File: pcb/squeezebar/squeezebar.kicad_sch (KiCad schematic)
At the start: 41 parts

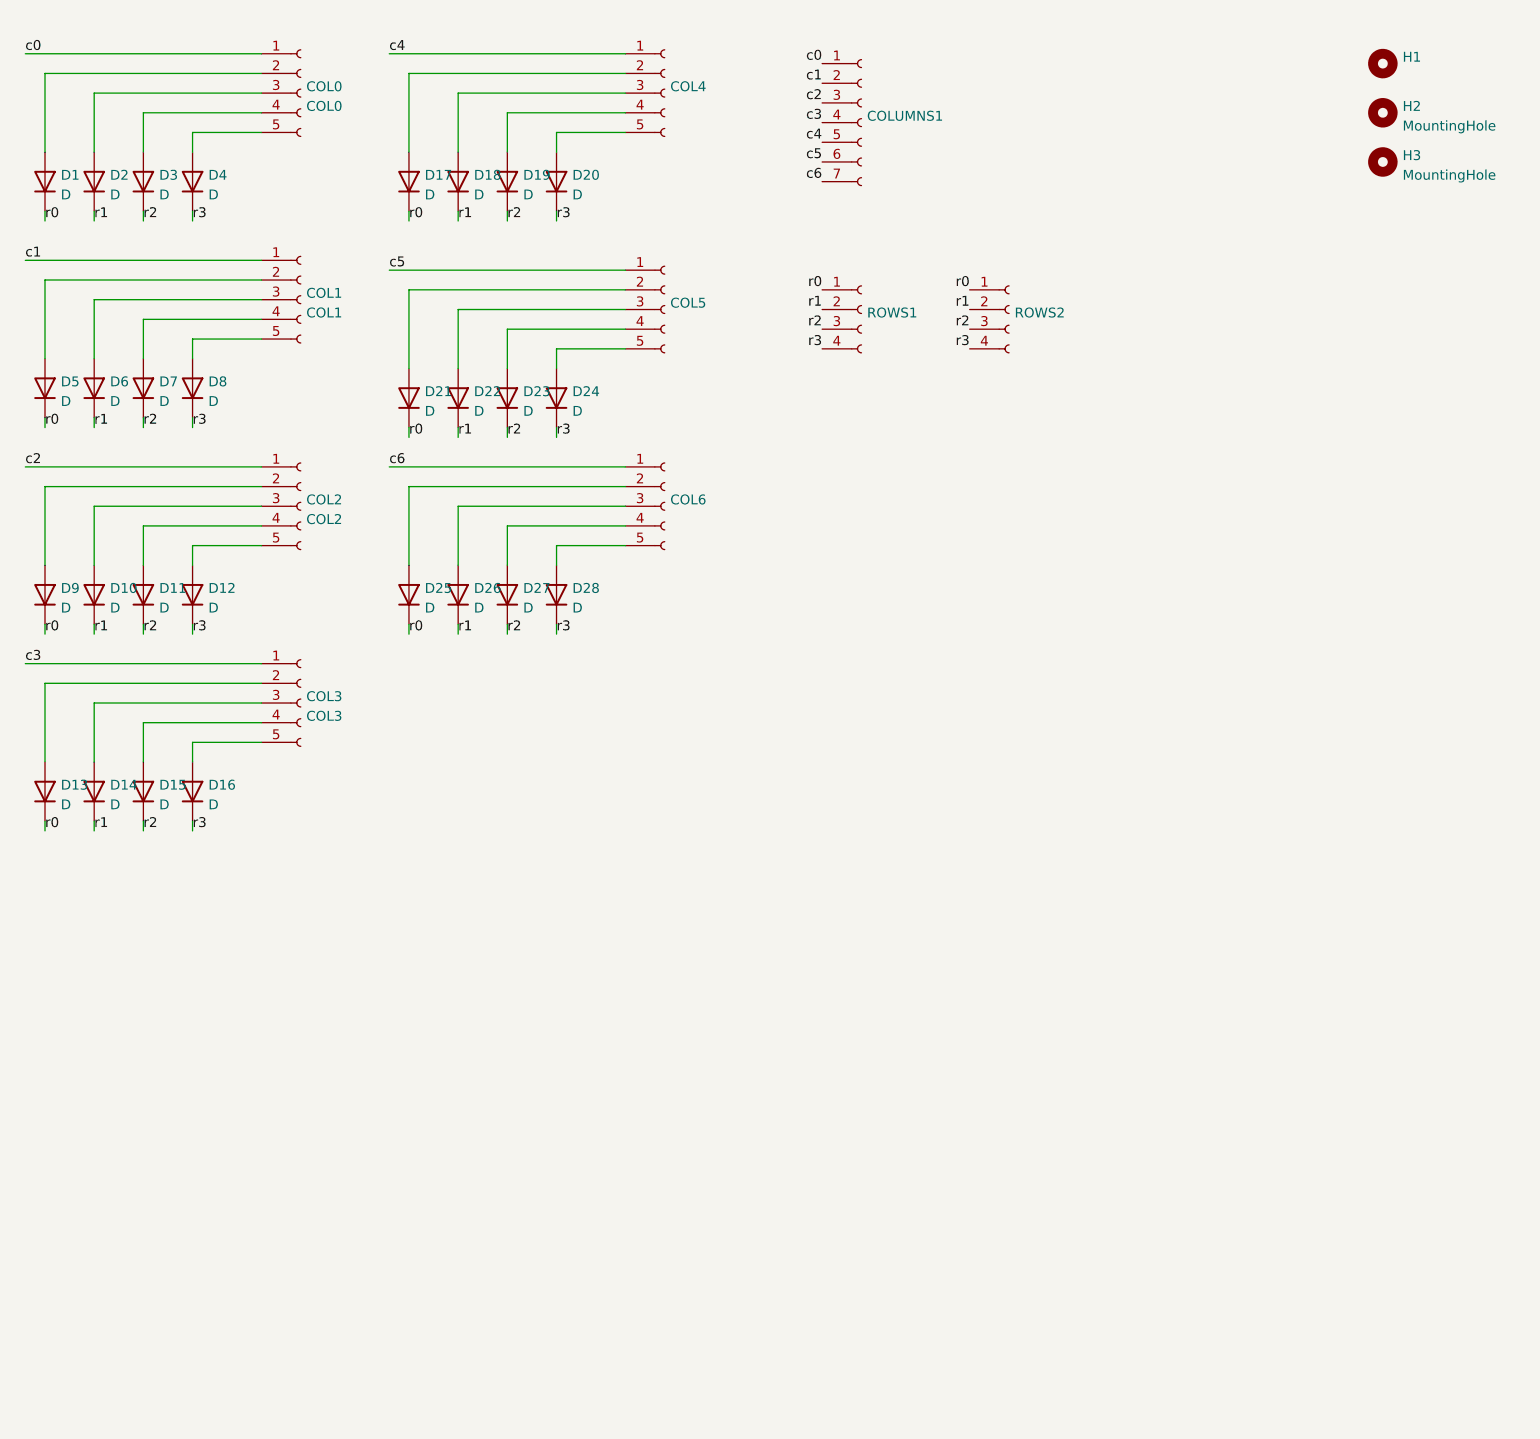
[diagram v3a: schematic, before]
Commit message: Squeezebar PCB: Add MCU. It's no longer a daughterboard...
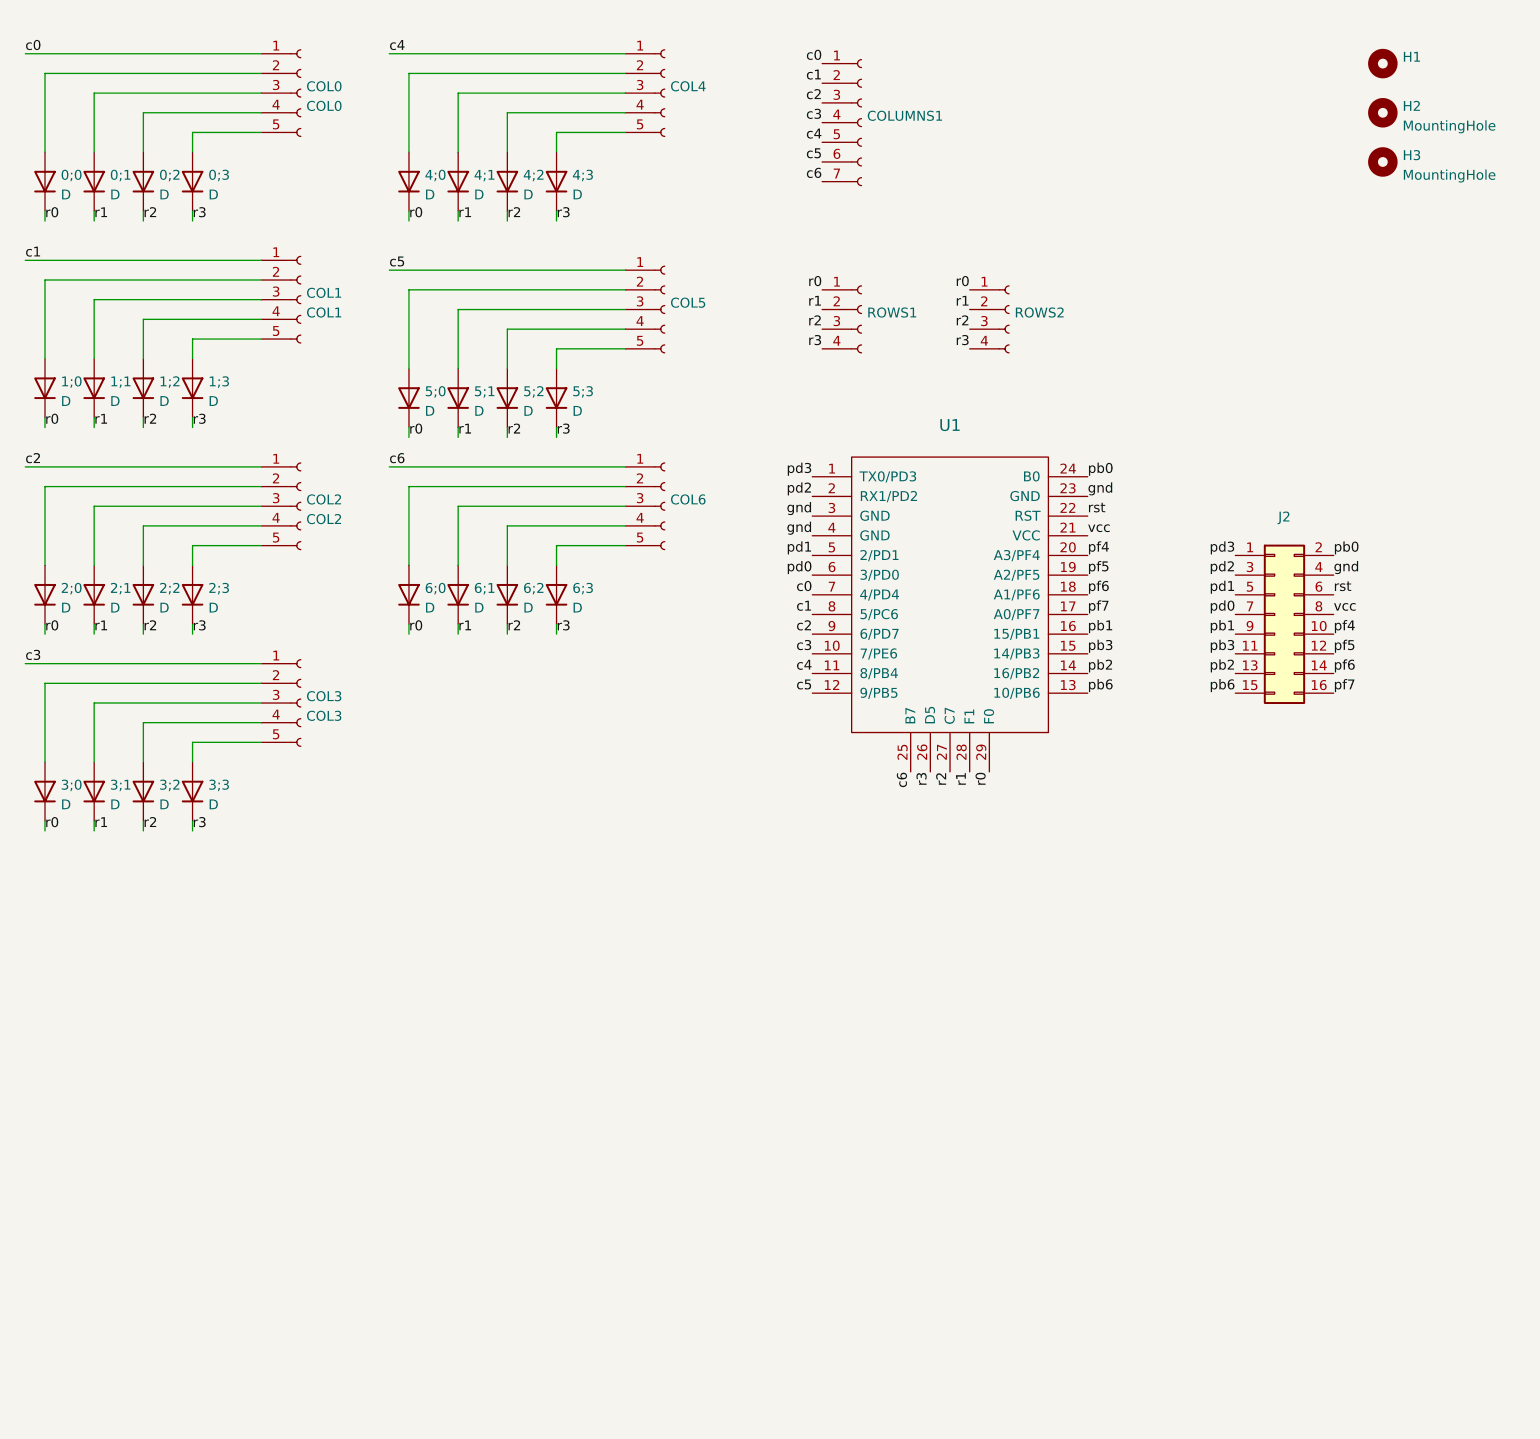
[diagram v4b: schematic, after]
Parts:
- added J2: (no value), symbol Connector_Generic:Conn_02x08_Odd_Even
- added U1: (no value), symbol keebio:Elite-C
- renumbered D1 to 0;0, D2 to 0;1, D3 to 0;2, D4 to 0;3, D5 to 1;0, D6 to 1;1, D7 to 1;2, D8 to 1;3, D9 to 2;0, D10 to 2;1, D11 to 2;2, D12 to 2;3, D13 to 3;0, D14 to 3;1, D15 to 3;2, D16 to 3;3, D17 to 4;0, D18 to 4;1, D19 to 4;2, D20 to 4;3, D21 to 5;0, D22 to 5;1, D23 to 5;2, D24 to 5;3, D25 to 6;0, D26 to 6;1, D27 to 6;2, D28 to 6;3
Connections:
- net c0: now also U1.7 (4/PD4)
- net c1: now also U1.8 (5/PC6)
- net c2: now also U1.9 (6/PD7)
- net c3: now also U1.10 (7/PE6)
- net c4: now also U1.11 (8/PB4)
- net c5: now also U1.12 (9/PB5)
- net c6: now also U1.25 (B7)
- net r0: now also U1.29 (F0)
- net r1: now also U1.28 (F1)
- net r2: now also U1.27 (C7)
- net r3: now also U1.26 (D5)
- new net gnd: J2.4 (Pin_4), U1.23 (GND), U1.3 (GND), U1.4 (GND)
- new net pb0: J2.2 (Pin_2), U1.24 (B0)
- new net pb1: J2.9 (Pin_9), U1.16 (15/PB1)
- new net pb2: J2.13 (Pin_13), U1.14 (16/PB2)
- new net pb3: J2.11 (Pin_11), U1.15 (14/PB3)
- new net pb6: J2.15 (Pin_15), U1.13 (10/PB6)
- new net pd0: J2.7 (Pin_7), U1.6 (3/PD0)
- new net pd1: J2.5 (Pin_5), U1.5 (2/PD1)
- new net pd2: J2.3 (Pin_3), U1.2 (RX1/PD2)
- new net pd3: J2.1 (Pin_1), U1.1 (TX0/PD3)
- new net pf4: J2.10 (Pin_10), U1.20 (A3/PF4)
- new net pf5: J2.12 (Pin_12), U1.19 (A2/PF5)
- new net pf6: J2.14 (Pin_14), U1.18 (A1/PF6)
- new net pf7: J2.16 (Pin_16), U1.17 (A0/PF7)
- new net rst: J2.6 (Pin_6), U1.22 (RST)
- new net vcc: J2.8 (Pin_8), U1.21 (VCC)

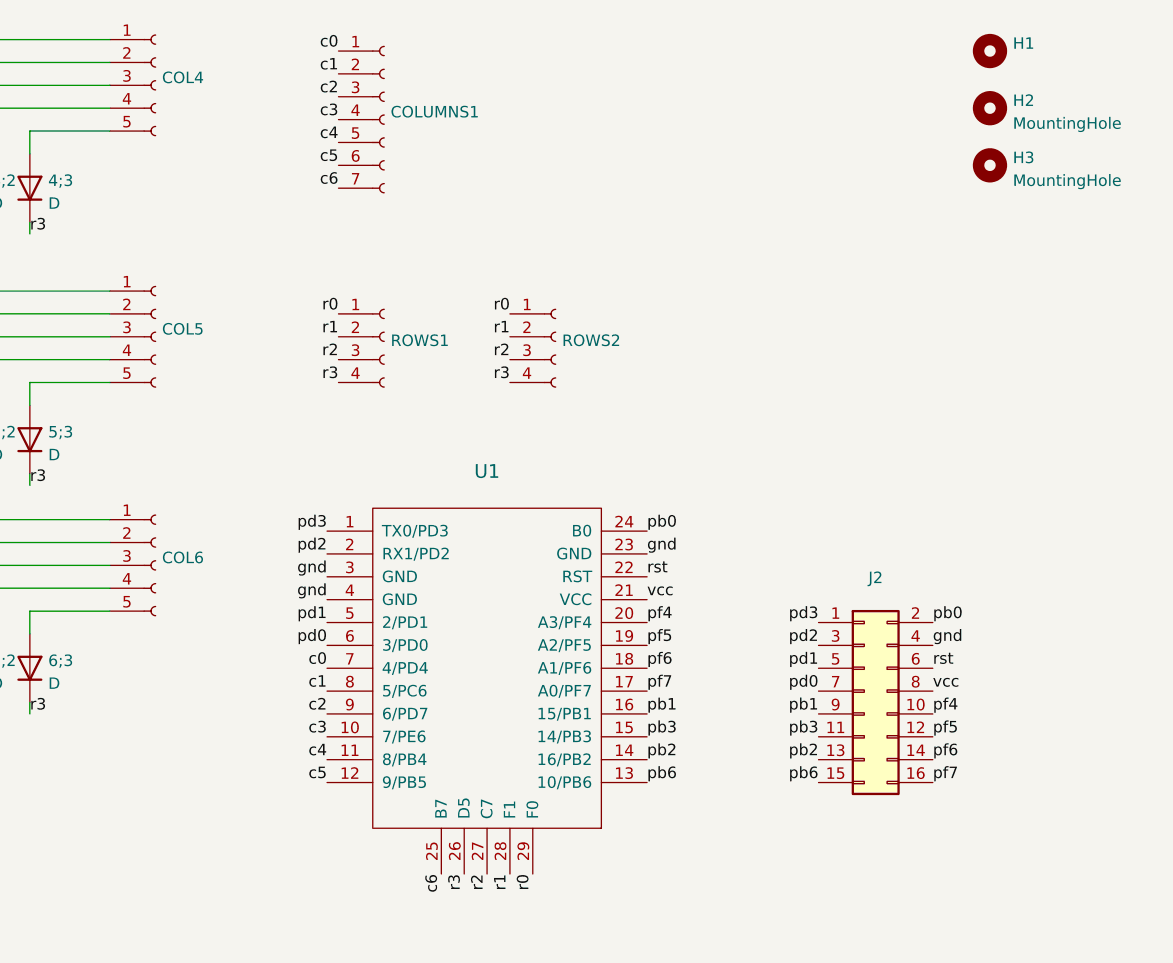
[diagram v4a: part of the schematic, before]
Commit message: MatrixBar: Use Pro Micro pins for the rows/cols
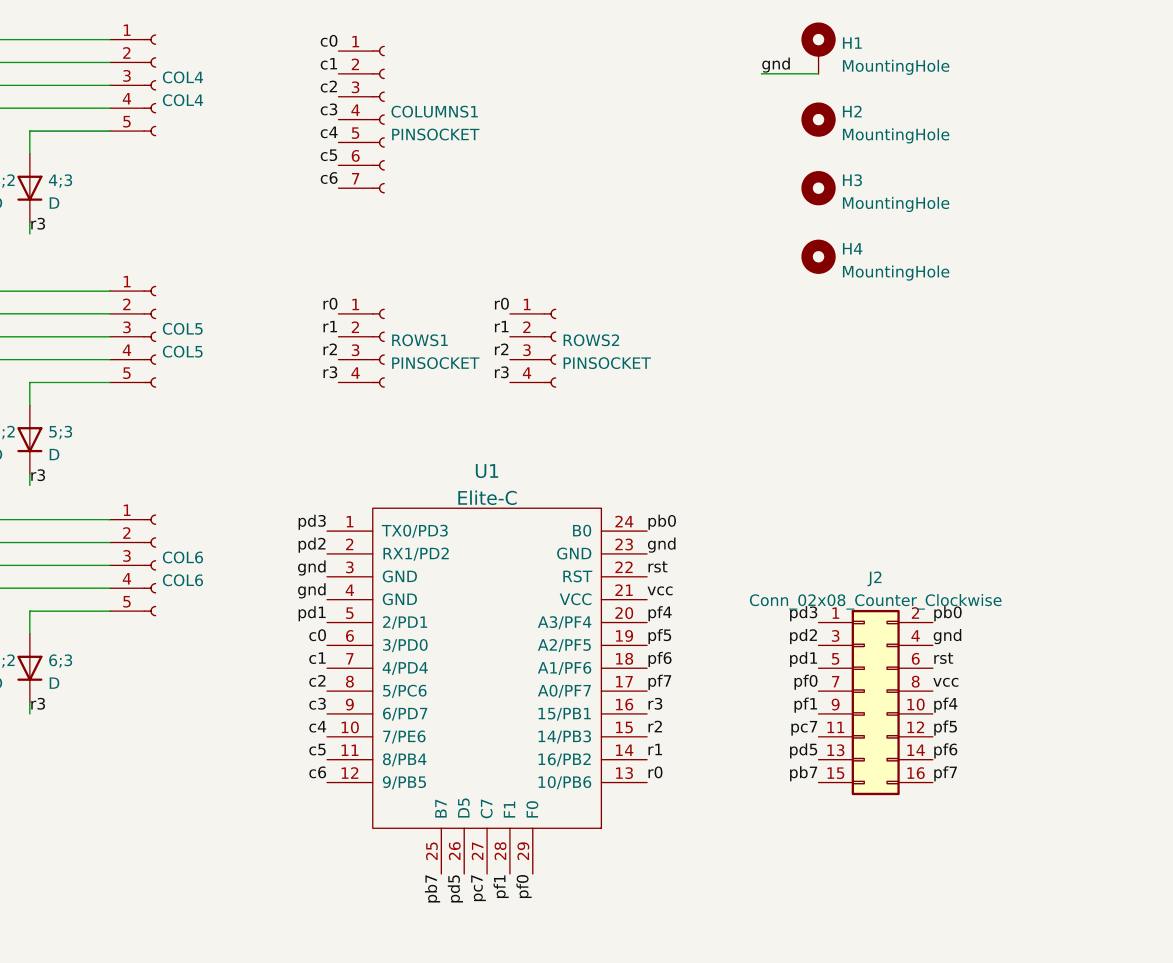
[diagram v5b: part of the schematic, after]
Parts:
- added H4: MountingHole, symbol Mechanical:MountingHole
- 0;0, 0;1, 0;2, 0;3, 1;0, 1;1, 1;2, 1;3, 2;0, 2;1, 2;2, 2;3, 3;0, 3;1, 3;2, 3;3, 4;0, 4;1, 4;2, 4;3, 5;0, 5;1, 5;2, 5;3, 6;0, 6;1, 6;2, 6;3: footprint (none) -> Library:Diode
- COL4: value (none) -> COL4
- COL5: value (none) -> COL5
- COL6: value (none) -> COL6
- COLUMNS1: value (none) -> PINSOCKET; footprint (none) -> Connector_PinHeader_2.54mm:PinHeader_1x07_P2.54mm_Vertical
- H1: value (none) -> MountingHole; footprint (none) -> MountingHole:MountingHole_2.2mm_M2_DIN965_Pad; symbol Mechanical:MountingHole -> Mechanical:MountingHole_Pad
- H3: footprint MountingHole:MountingHole_2.2mm_M2_DIN965 -> (none)
- J2: value (none) -> Conn_02x08_Counter_Clockwise; footprint (none) -> Library:PinSocket_2x08_P2.54mm_Bespoke
- ROWS1, ROWS2: value (none) -> PINSOCKET; footprint (none) -> Library:PinSocket_1x04_P2.54mm_Vertical_LongPads
- U1: value (none) -> Elite-C; footprint (none) -> 3dmodels:Elite-C
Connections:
- net c0: now also U1.6 (3/PD0); no longer U1.7 (4/PD4)
- net c1: now also U1.7 (4/PD4); no longer U1.8 (5/PC6)
- net c2: now also U1.8 (5/PC6); no longer U1.9 (6/PD7)
- net c3: now also U1.9 (6/PD7); no longer U1.10 (7/PE6)
- net c4: now also U1.10 (7/PE6); no longer U1.11 (8/PB4)
- net c5: now also U1.11 (8/PB4); no longer U1.12 (9/PB5)
- net c6: now also U1.12 (9/PB5); no longer U1.25 (B7)
- net gnd: now also H1.1
- net r0: now also U1.13 (10/PB6); no longer U1.29 (F0)
- net r1: now also U1.14 (16/PB2); no longer U1.28 (F1)
- net r2: now also U1.15 (14/PB3); no longer U1.27 (C7)
- net r3: now also U1.16 (15/PB1); no longer U1.26 (D5)
- net pb1 renamed pf1
- net pf1: now also U1.28 (F1); no longer U1.16 (15/PB1)
- net pb2 renamed pd5
- net pd5: now also U1.26 (D5); no longer U1.14 (16/PB2)
- net pb3 renamed pc7
- net pc7: now also U1.27 (C7); no longer U1.15 (14/PB3)
- net pb6 renamed pb7
- net pb7: now also U1.25 (B7); no longer U1.13 (10/PB6)
- net pd0 renamed pf0
- net pf0: now also U1.29 (F0); no longer U1.6 (3/PD0)
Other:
- moved on the sheet: H2, H3

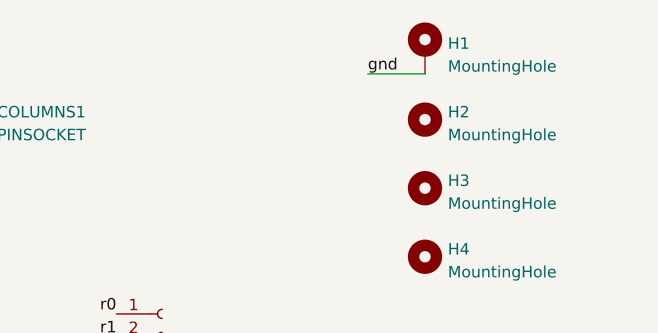
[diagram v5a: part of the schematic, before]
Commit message: Switch to M3 screws
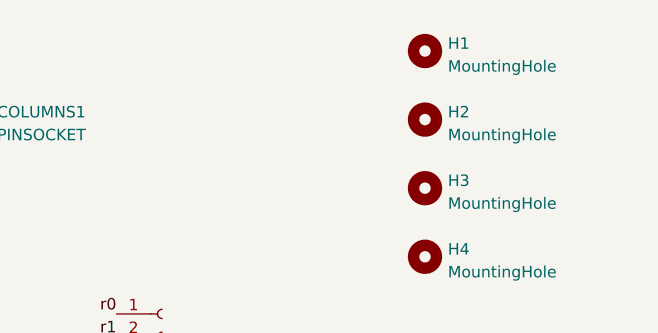
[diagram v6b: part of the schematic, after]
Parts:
- H1: footprint MountingHole:MountingHole_2.2mm_M2_DIN965_Pad -> (none); symbol Mechanical:MountingHole_Pad -> Mechanical:MountingHole
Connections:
- net gnd: no longer H1.1
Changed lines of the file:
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@@
-    (stroke (width 0) (type default) (color 0 0 0 0))
-  )
-  (wire (pts (xy 171.45 24.13) (xy 177.8 24.13))
     (stroke (width 0) (type default) (color 0 0 0 0))
   )
@@
   )
   (label "r3" (at 43.18 41.91 0)
-    (effects (font (size 1.27 1.27)) (justify left bottom))
-  )
-  (label "gnd" (at 171.45 24.13 0)
     (effects (font (size 1.27 1.27)) (justify left bottom))
   )
@@
     (pin "2")
   )
-  (symbol (lib_id "Mechanical:MountingHole_Pad") (at 177.8 21.59 0) (unit 1)
+  (symbol (lib_id "Mechanical:MountingHole") (at 177.8 21.59 0) (unit 1)
     (in_bom yes) (on_board yes) (fields_autoplaced)
     (property "Reference" "H1" (id 0) (at 180.34 20.7553 0)
@@
       (effects (font (size 1.27 1.27)) (justify left))
     )
-    (property "Footprint" "MountingHole:MountingHole_2.2mm_M2_DIN965_Pad" (id 2) (at 177.8 21.59 0)
+    (property "Footprint" "" (id 2) (at 177.8 21.59 0)
       (effects (font (size 1.27 1.27)) hide)
     )
@@
       (effects (font (size 1.27 1.27)) hide)
     )
-    (pin "1")
   )
   (symbol (lib_id "Connector:Conn_01x07_Female") (at 129.54 29.21 0) (unit 1)
@@
     )
     (path "/4a7faed8-406c-419a-aaa0-2e6ca12fec45"
-      (reference "H1") (unit 1) (value "MountingHole") (footprint "MountingHole:MountingHole_2.2mm_M2_DIN965_Pad")
+      (reference "H1") (unit 1) (value "MountingHole") (footprint "MountingHole:MountingHole_3.2mm_M3_DIN965")
     )
     (path "/9de285d6-22fe-43e5-9255-2df4222a64a4"
-      (reference "H2") (unit 1) (value "MountingHole") (footprint "MountingHole:MountingHole_2.2mm_M2_DIN965")
+      (reference "H2") (unit 1) (value "MountingHole") (footprint "MountingHole:MountingHole_3.2mm_M3_DIN965")
     )
     (path "/bb57eb3d-1745-47c0-80c3-5875a3e120da"
-      (reference "H3") (unit 1) (value "MountingHole") (footprint "MountingHole:MountingHole_2.2mm_M2_DIN965")
+      (reference "H3") (unit 1) (value "MountingHole") (footprint "MountingHole:MountingHole_3.2mm_M3_DIN965")
     )
     (path "/e78d8360-845a-4e52-a48a-372ed98ff282"
-      (reference "H4") (unit 1) (value "MountingHole") (footprint "MountingHole:MountingHole_2.2mm_M2_DIN965")
+      (reference "H4") (unit 1) (value "MountingHole") (footprint "MountingHole:MountingHole_3.2mm_M3_DIN965")
     )
     (path "/66a7b41e-febe-411e-979f-084594b3b8e3"
